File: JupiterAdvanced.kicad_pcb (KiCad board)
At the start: 2 copper layers, 314.8 x 165.9 mm, 224 parts, among them SW1 SW_Push, U1 PRTR5V0U2X, U10 ATmega32U4-AU, Y1 16MHz

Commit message: JLCPCB W202105121404401
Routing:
- net +5V: track 102.7 -> 125.4 mm, vias 3 -> 5

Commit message: Minor adjustments
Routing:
- net Earth: track 3.21 -> 11.1 mm, vias 3 -> 4
- net GND: track 155.1 -> 157.7 mm

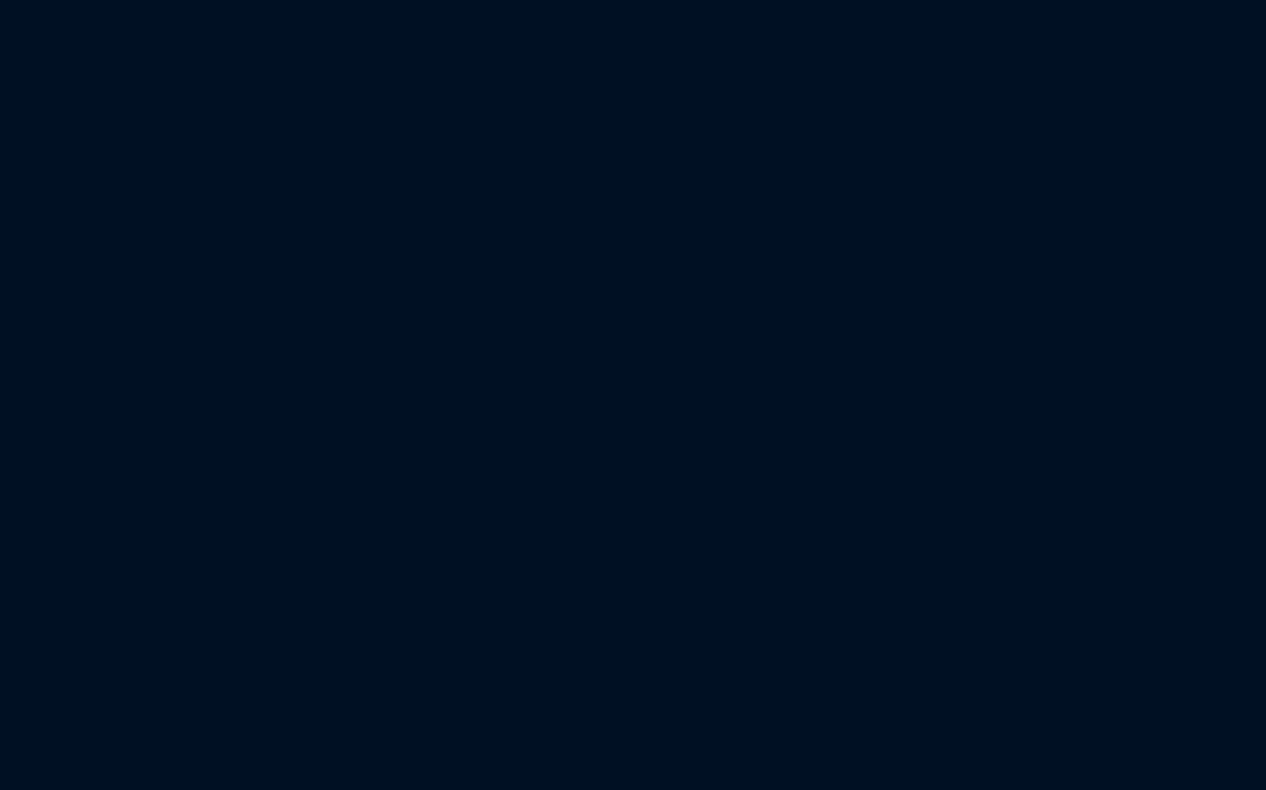
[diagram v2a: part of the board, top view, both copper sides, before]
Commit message: UnderGlow added, not yet routed
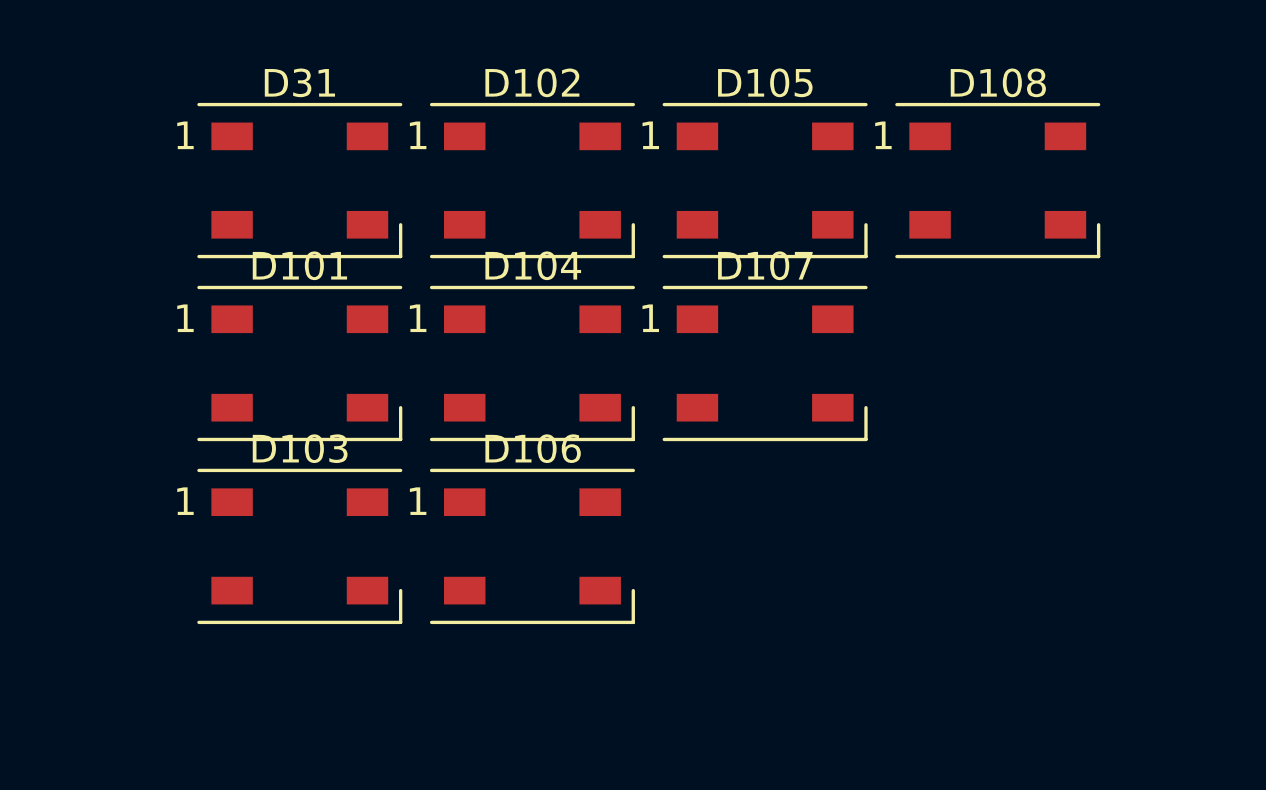
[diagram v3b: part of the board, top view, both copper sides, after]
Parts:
- added D101: WS2812B, LED_SMD:LED_WS2812B_PLCC4_5.0x5.0mm_P3.2mm, F.Cu at (166.8, 54.9)
- added D102: WS2812B, LED_SMD:LED_WS2812B_PLCC4_5.0x5.0mm_P3.2mm, F.Cu at (175.2, 48.3)
- added D103: WS2812B, LED_SMD:LED_WS2812B_PLCC4_5.0x5.0mm_P3.2mm, F.Cu at (166.8, 61.5)
- added D104: WS2812B, LED_SMD:LED_WS2812B_PLCC4_5.0x5.0mm_P3.2mm, F.Cu at (175.2, 54.9)
- added D105: WS2812B, LED_SMD:LED_WS2812B_PLCC4_5.0x5.0mm_P3.2mm, F.Cu at (183.7, 48.3)
- added D106: WS2812B, LED_SMD:LED_WS2812B_PLCC4_5.0x5.0mm_P3.2mm, F.Cu at (175.2, 61.5)
- added D107: WS2812B, LED_SMD:LED_WS2812B_PLCC4_5.0x5.0mm_P3.2mm, F.Cu at (183.7, 54.9)
- added D108: WS2812B, LED_SMD:LED_WS2812B_PLCC4_5.0x5.0mm_P3.2mm, F.Cu at (192.1, 48.3)
- added D31: WS2812B, LED_SMD:LED_WS2812B_PLCC4_5.0x5.0mm_P3.2mm, F.Cu at (166.8, 48.3)
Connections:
- U10 pad 1: Net-(U10-Pad1) -> LED

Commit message: GND Pours added
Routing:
- net GND: vias 9 -> 71

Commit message: Push Switch updated, Underglow LED work started
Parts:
- removed D107, D108, D31: WS2812B, LED_SMD:LED_WS2812B_PLCC4_5.0x5.0mm_P3.2mm
- added BLD1: WS2812B, LED_SMD:LED_WS2812B_PLCC4_5.0x5.0mm_P3.2mm, B.Cu at (344.4, 86.4)
- BLD2: renamed from D101; moved to B.Cu
- BLD3: renamed from D102; moved to B.Cu
- BLD4: renamed from D103; moved to B.Cu
- BLD5: renamed from D104; moved to B.Cu
- BLD6: renamed from D105; moved to B.Cu
- BLD7: renamed from D106; moved to B.Cu
- SW1: footprint JupiterAdvancedKbd_localFP:TS-1187A-B-A-B -> Button_Switch_SMD:SW_SPST_SKQG_WithoutStem
- moved BLD2 135.6 mm to (298.7, 86.4)
- moved BLD7 87.9 mm to (90.9, 86.4)
- moved BLD3 68.5 mm to (232.1, 86.4)
- moved BLD6 61.4 mm to (135.6, 86.4)
- moved BLD4 44.9 mm to (204.2, 86.4)
- moved BLD5 33.6 mm to (163.5, 86.4)
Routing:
- net Net-(BLD6-Pad2): track 0.00 -> 41.1 mm
- net Net-(BLD4-Pad2): track 0.00 -> 37.1 mm
- net Net-(BLD3-Pad2): track 0.00 -> 24.4 mm
- net Net-(BLD5-Pad2): track 0.00 -> 24.4 mm
- net GND: track 157.7 -> 145.7 mm
- net Net-(R8-Pad2): track 34.3 -> 26.7 mm

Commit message: Underglow Work continued
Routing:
- net +5V: track 125.4 -> 192.9 mm, vias 5 -> 7
- net Net-(BLD1-Pad2): track 0.00 -> 42.1 mm

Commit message: Underglow Routing Complete
Underglow routing is complete, but must be reworked for routing esthetics.
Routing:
- net Net-(BLD2-Pad2): track 0.00 -> 218.2 mm, vias 0 -> 14
- net +5V: track 192.9 -> 384.8 mm
- net LED: track 0.00 -> 189.2 mm, vias 0 -> 6
